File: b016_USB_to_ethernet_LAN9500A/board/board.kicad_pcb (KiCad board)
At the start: 4 copper layers, 21 x 29 mm, 28 parts, among them J1 008_USB_2x2, J2 009_1000BASE-T_2x5, U1 LAN9500(A), Y1 25MhZ

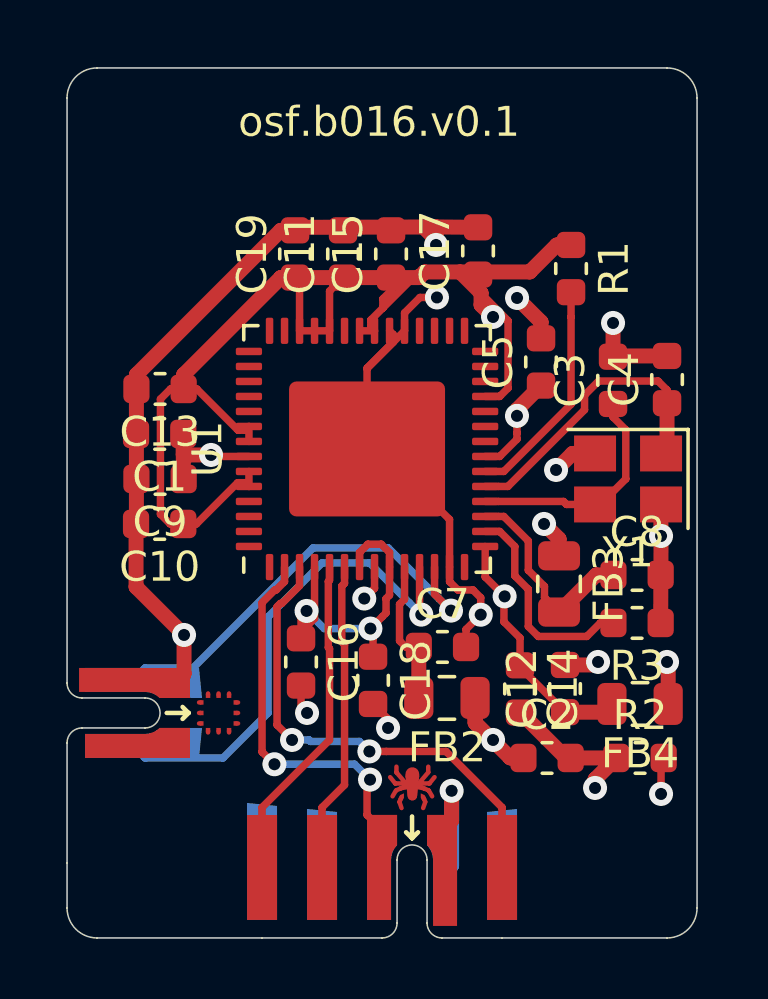
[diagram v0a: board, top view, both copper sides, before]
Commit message: added EEPROM, modernized connectors. still needs LDO
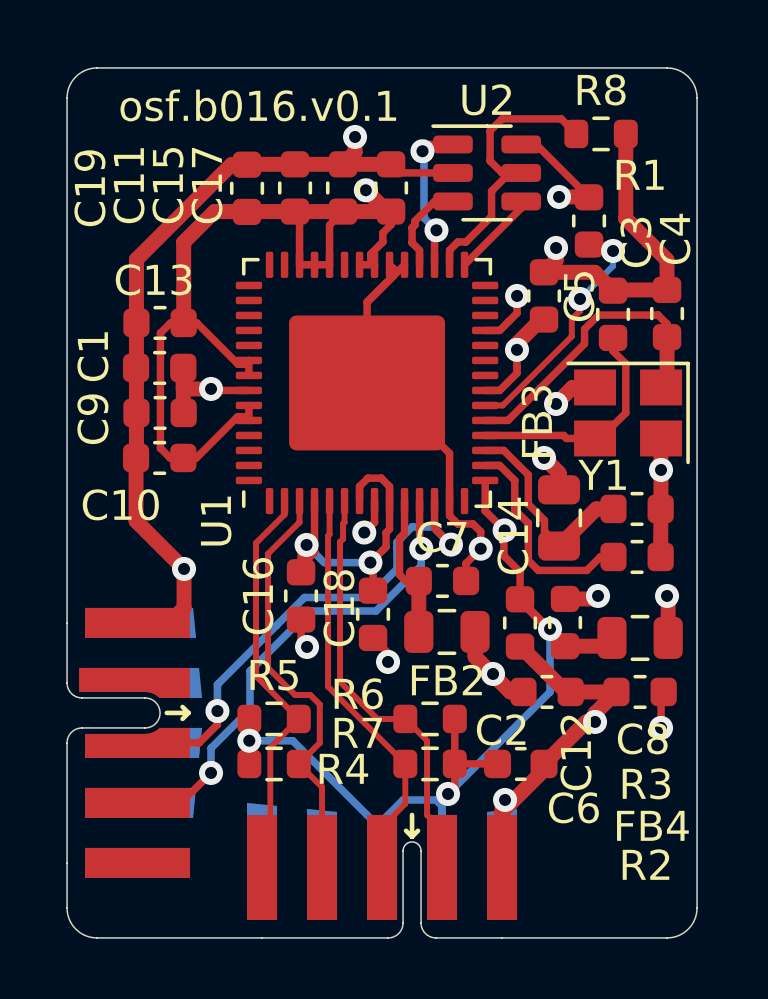
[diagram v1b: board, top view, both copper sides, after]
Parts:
- added C6: 100nF, Capacitor_SMD:C_0603_1608Metric, F.Cu at (145.1, 107.2)
- added R4: 49.9R, Resistor_SMD:R_0603_1608Metric, F.Cu at (136.9, 107.2)
- added R5: 49.9R, Resistor_SMD:R_0603_1608Metric, F.Cu at (136.9, 105.7)
- added R6: 49.9R, Resistor_SMD:R_0603_1608Metric, F.Cu at (142.1, 105.7)
- added R7: 49.9R, Resistor_SMD:R_0603_1608Metric, F.Cu at (142.1, 107.2)
- added R8: 12k, Resistor_SMD:R_0603_1608Metric, F.Cu at (147.8, 86.2)
- added U2: 93AA56AT-I/OT, Package_TO_SOT_SMD:SOT-23-6, F.Cu at (144.0, 87.5)
- J1: footprint on_edge:on_edge_2x02_device -> on_edge:on_edge_2x05_device
- moved C17 7.98 mm to (136.0, 88.0)
- moved C5 2.20 mm to (145.9, 91.6)
- moved C1 2.20 mm to (133.1, 94.0)
- moved C10 2.20 mm to (133.1, 97.0)
- moved C11 2.20 mm to (139.2, 88.0)
- moved C12 2.20 mm to (146.6, 102.5)
- moved C13 2.20 mm to (133.1, 92.5)
- moved C14 2.20 mm to (145.1, 102.5)
- moved C15 2.20 mm to (140.8, 88.0)
- moved C16 2.20 mm to (137.8, 101.6)
- moved C19 2.20 mm to (137.6, 88.0)
- moved C2 2.20 mm to (146.0, 104.8)
- moved C4 2.20 mm to (150.0, 92.2)
- moved C7 2.20 mm to (142.5, 101.1)
- moved C8 2.20 mm to (149.0, 98.7)
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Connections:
- C12 pad 1: Net-(C12-Pad1) -> /Sheet603703E3/CT1
- C14 pad 1: Net-(C12-Pad1) -> /Sheet603703E3/CT1
- C16 pad 1: Net-(C12-Pad1) -> /Sheet603703E3/CT1
- C18 pad 1: Net-(C12-Pad1) -> /Sheet603703E3/CT1
- FB4 pad 2: Net-(C12-Pad1) -> /Sheet603703E3/CT1
- J1 pad 2: (no net) -> /VCC
- J2 pad 2: /Sheet603703E3/D1- -> /Sheet603703E3/D2+
- J2 pad 3: GND -> /Sheet603703E3/D2-
- J2 pad 4: (no net) -> /Sheet603703E3/D1+
- J2 pad 5: /Sheet603703E3/D2+ -> /Sheet603703E3/D1-
- J2 pad 6: (no net) -> GND
- J2 pad 7: /Sheet603703E3/D1+ -> /Sheet603703E3/CT1
- J2 pad 8: (no net) -> /Sheet603703E3/CT1
- J2 pad 9: /Sheet603703E3/D2- -> (no net)
- U1 pad 1: (no net) -> unconnected-(U1-Pad1)
- U1 pad 14: (no net) -> unconnected-(U1-Pad14)
- U1 pad 15: Net-(C12-Pad1) -> /Sheet603703E3/CT1
- U1 pad 22: (no net) -> unconnected-(U1-Pad22)
- U1 pad 23: (no net) -> unconnected-(U1-Pad23)
- U1 pad 24: (no net) -> unconnected-(U1-Pad24)
- U1 pad 26: (no net) -> unconnected-(U1-Pad26)
- U1 pad 27: (no net) -> unconnected-(U1-Pad27)
- U1 pad 28: (no net) -> unconnected-(U1-Pad28)
- U1 pad 29: (no net) -> Net-(U1-Pad29)
- U1 pad 30: (no net) -> Net-(U1-Pad30)
- U1 pad 31: (no net) -> Net-(U1-Pad31)
- U1 pad 32: (no net) -> Net-(U1-Pad32)
- U1 pad 37: (no net) -> unconnected-(U1-Pad37)
- U1 pad 4: Net-(C12-Pad1) -> /Sheet603703E3/CT1
- U1 pad 41: (no net) -> unconnected-(U1-Pad41)
- U1 pad 42: (no net) -> unconnected-(U1-Pad42)
- U1 pad 43: (no net) -> unconnected-(U1-Pad43)
- U1 pad 44: (no net) -> unconnected-(U1-Pad44)
- U1 pad 45: (no net) -> unconnected-(U1-Pad45)
- U1 pad 46: (no net) -> unconnected-(U1-Pad46)
- U1 pad 47: (no net) -> unconnected-(U1-Pad47)
- U1 pad 53: (no net) -> unconnected-(U1-Pad53)
- U1 pad 54: (no net) -> unconnected-(U1-Pad54)
- U1 pad 55: (no net) -> unconnected-(U1-Pad55)
- U1 pad 56: (no net) -> unconnected-(U1-Pad56)
- U1 pad 7: Net-(C12-Pad1) -> /Sheet603703E3/CT1
- U1 pad 9: Net-(C12-Pad1) -> /Sheet603703E3/CT1
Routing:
- net /Sheet603703E3/CT1: track 0.00 -> 55.0 mm, vias 0 -> 6
- net Net-(C12-Pad1): track 24.9 -> 0.00 mm, vias 3 -> 0
- net Net-(U1-Pad30): track 0.00 -> 9.89 mm
- net Net-(U1-Pad31): track 0.00 -> 5.11 mm, vias 0 -> 2
- net Net-(U1-Pad32): track 0.00 -> 3.14 mm
- net Net-(U1-Pad29): track 0.00 -> 2.89 mm
- net /Sheet603703E3/D2+: track 10.4 -> 13.0 mm
- net GND: track 118.8 -> 116.7 mm, vias 13 -> 11
- net /Sheet603703E3/D1+: track 16.2 -> 14.3 mm, vias 2 -> 0
- net /Sheet603703E3/D2-: track 11.0 -> 12.4 mm
- net /Sheet603703E3/D1-: track 12.4 -> 13.7 mm, vias 2 -> 0
- net /Sheet603703E3/DM: track 16.8 -> 16.1 mm, vias 1 -> 2
- net Net-(R1-Pad2): track 7.53 -> 8.15 mm, vias 0 -> 2
- net /Sheet603703E3/DP: track 15.1 -> 15.4 mm, vias 1 -> 2
- net +3V3: vias 2 -> 4
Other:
- outline, holes or cut-outs redrawn

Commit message: added LDO
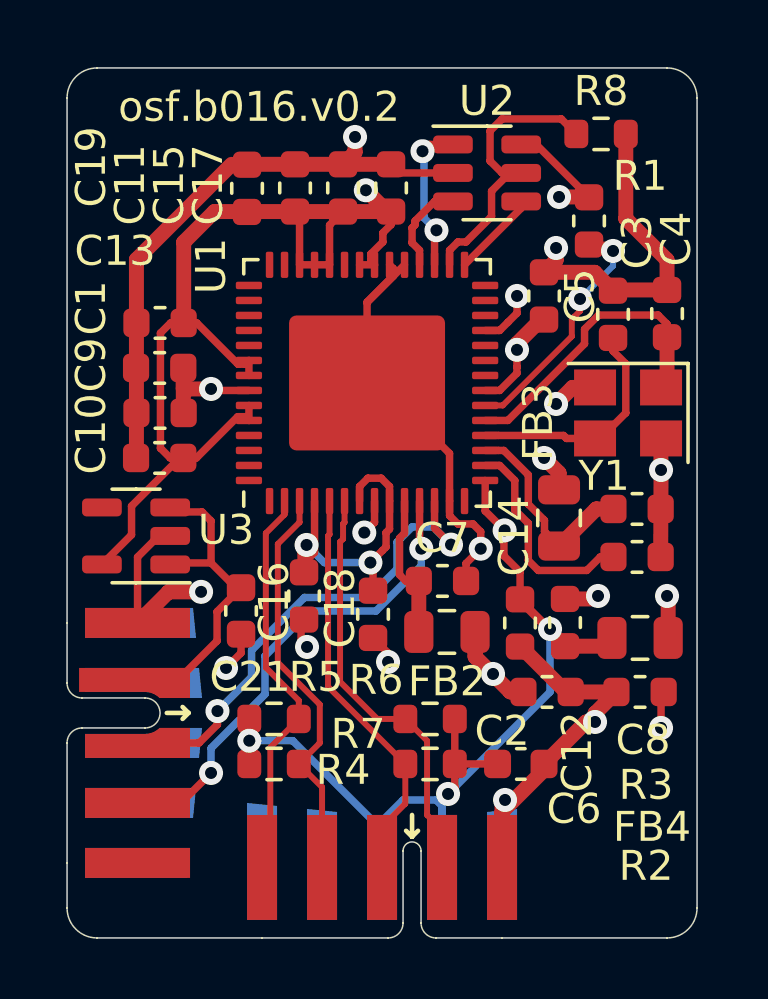
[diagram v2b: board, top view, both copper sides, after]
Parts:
- added C21: 1uF, Capacitor_SMD:C_0603_1608Metric, F.Cu at (135.8, 102.1)
- added U3: TC1017-xCT, Package_TO_SOT_SMD:SOT-23-5, F.Cu at (132.3, 99.6)
- moved C16 0.10 mm to (137.9, 101.6)
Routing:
- net /VCC: track 0.00 -> 9.76 mm
- net +3V3: track 60.6 -> 65.4 mm
- net GND: track 116.7 -> 118.4 mm, vias 11 -> 12
- net /Sheet603703E3/D1+: track 14.3 -> 13.7 mm
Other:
- board text added: "osf.b016.v0.2"
- board text removed: "osf.b016.v0.1"
